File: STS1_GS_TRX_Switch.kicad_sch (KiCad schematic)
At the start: 60 parts, among them J1 SDR, J10 PA_Switch, J11 LNA_Switch, J2 From_LNA, J3 To_PA, J4 To_LNA, J5 From_PA, J6 Antenna, J7 RX_LED, J8 TX_LED, J9 5V_Supply, K1 HF3-53, K2 HF3-53, K3 HF3-53, K4 IM07, K5 IM07, Q1 BC847, Q2 BC847, Q3 BC847, Q4 BC847, Q5 BC847, U1 PC817, U2 PC817

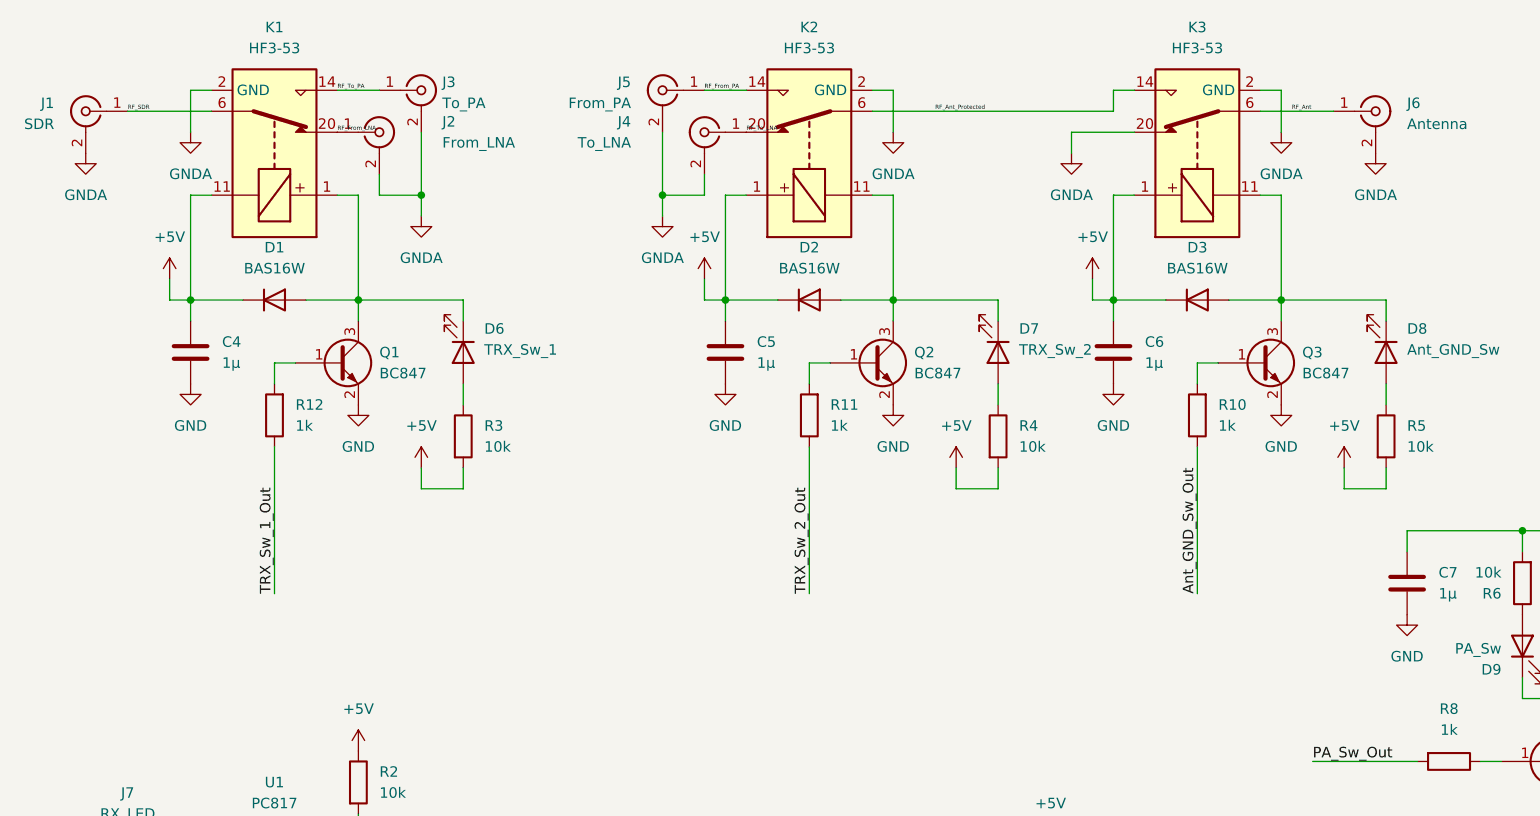
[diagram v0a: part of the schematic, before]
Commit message: fix: wrong polarity of one of the RF relays
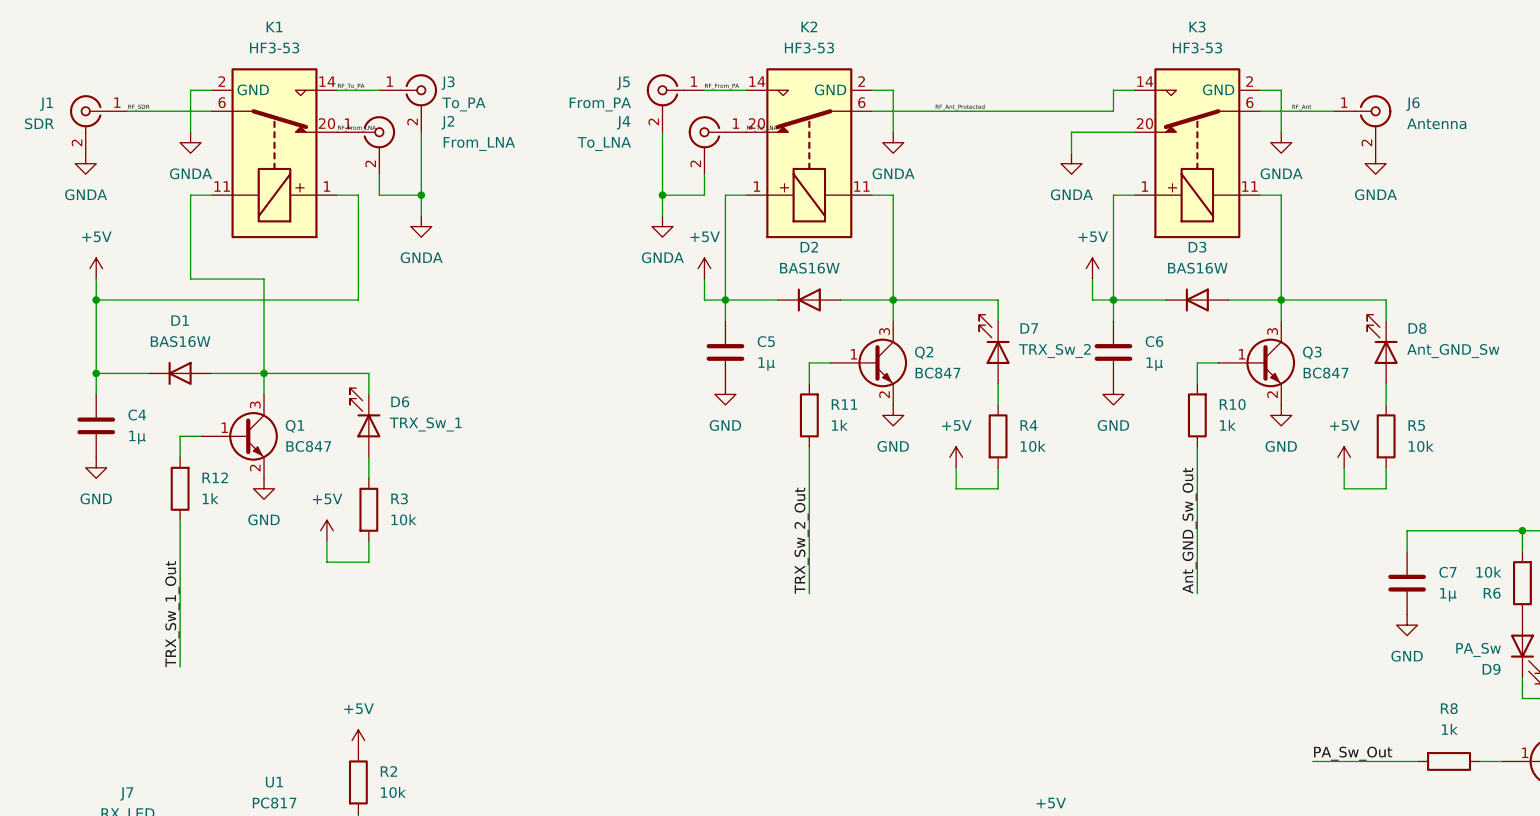
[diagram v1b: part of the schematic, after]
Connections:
- net +5V: now also K1.1; no longer K1.11
- net at D1.1 (A), D6.1 (K), Q1.3 (C): now also K1.11; no longer K1.1
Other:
- moved on the sheet: C4, D1, D6, Q1, R12, R3

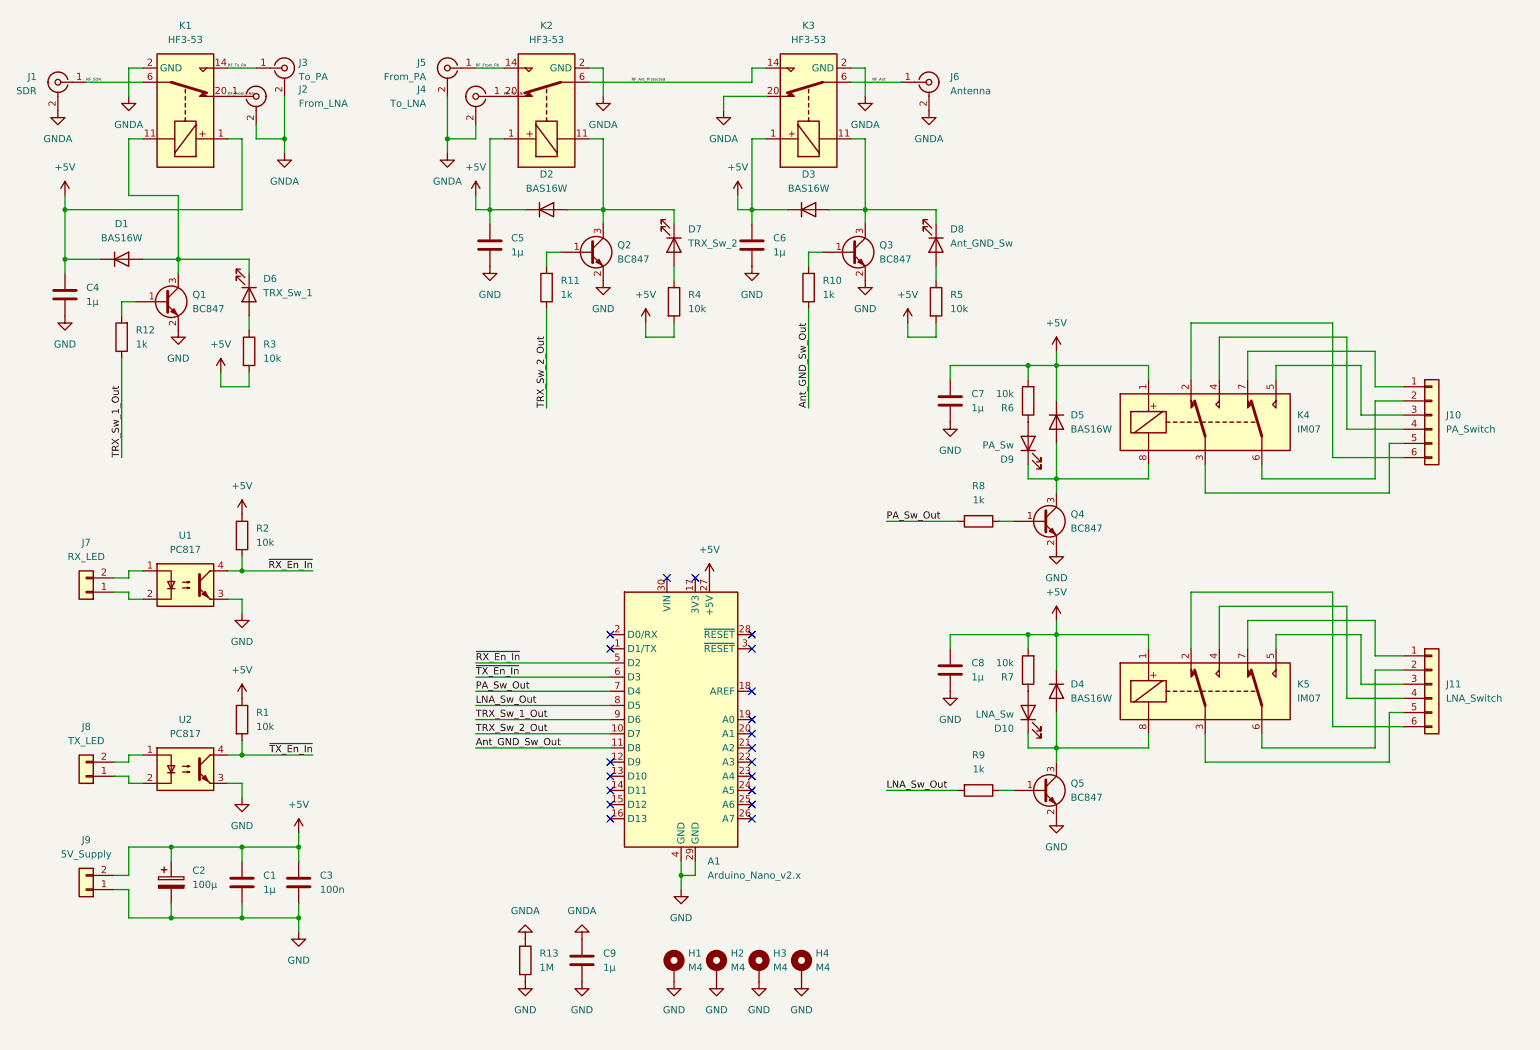
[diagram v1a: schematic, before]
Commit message: feat: v2.0 with built-in LNA, PA-pre-filter and PA output filter
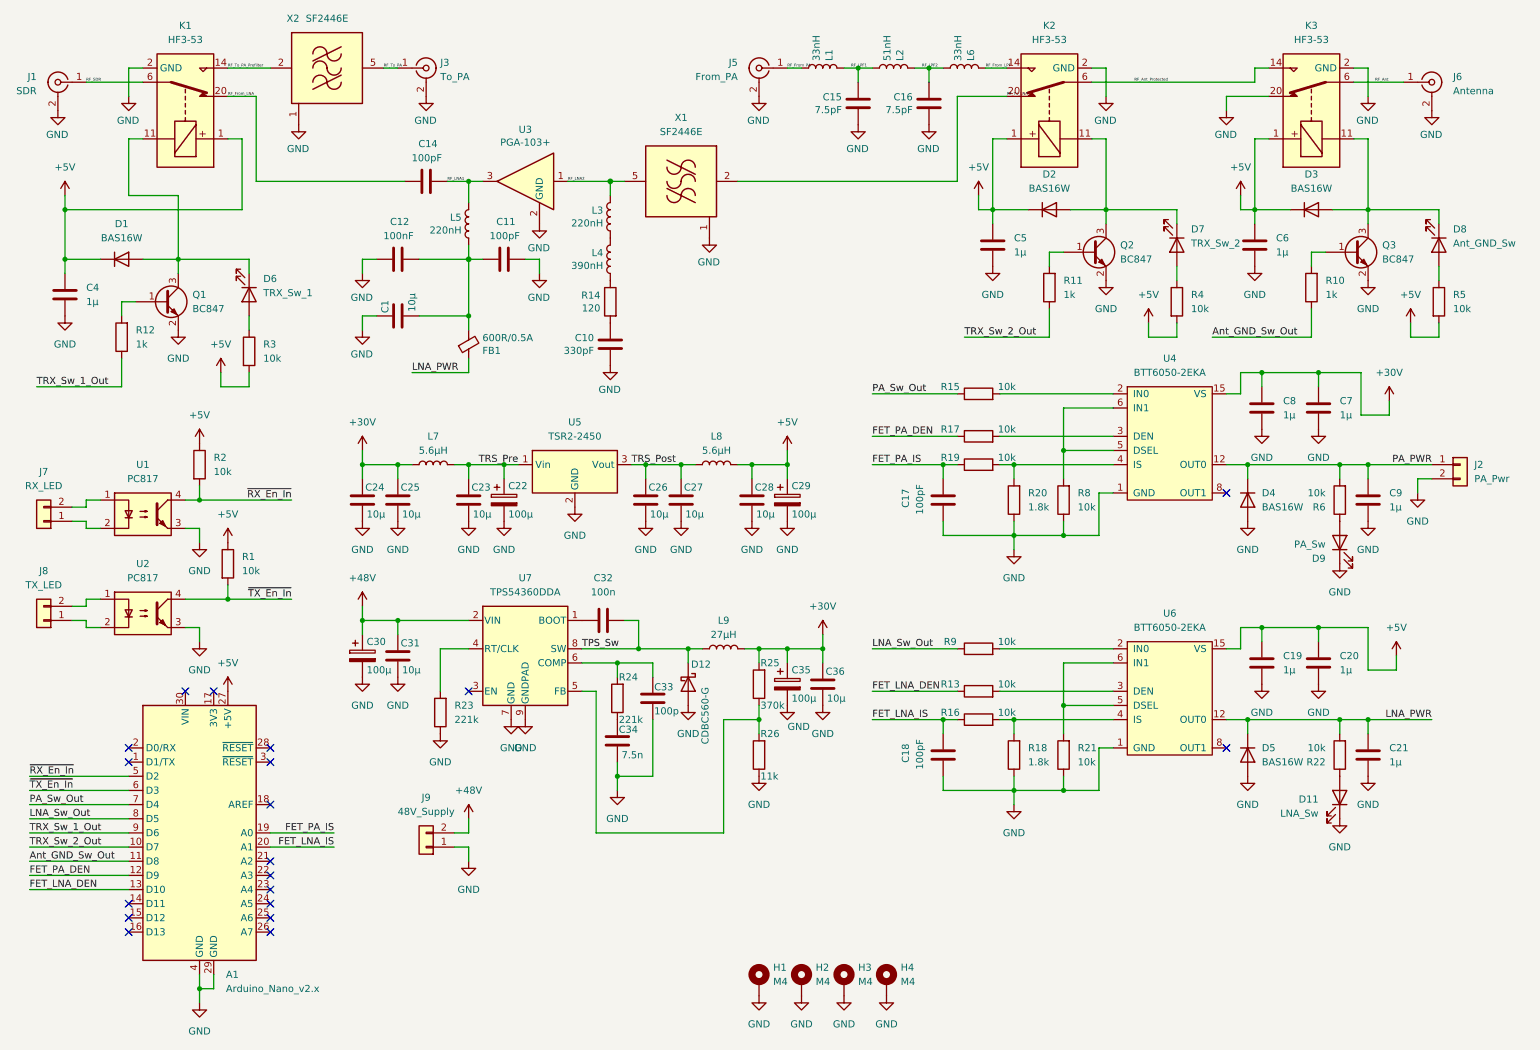
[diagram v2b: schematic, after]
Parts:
- removed C2: 100µ, Capacitor_SMD:CP_Elec_10x10, symbol Device:C_Polarized
- removed C3: 100n, Capacitor_SMD:C_0603_1608Metric_Pad1.08x0.95mm_HandSolder, symbol Device:C
- removed D10: LNA_Sw, LED_SMD:LED_1206_3216Metric_Pad1.42x1.75mm_HandSolder, symbol Device:LED
- removed J10: PA_Switch, Connector_JST:JST_XH_B6B-XH-A_1x06_P2.50mm_Vertical, symbol Connector_Generic:Conn_01x06
- removed J11: LNA_Switch, Connector_JST:JST_XH_B6B-XH-A_1x06_P2.50mm_Vertical, symbol Connector_Generic:Conn_01x06
- removed J2: From_LNA, Connector_Coaxial:SMA_Molex_73251-2120_EdgeMount_Horizontal, symbol Connector:Conn_Coaxial
- removed J4: To_LNA, Connector_Coaxial:SMA_Molex_73251-2120_EdgeMount_Horizontal, symbol Connector:Conn_Coaxial
- removed K4, K5: IM07, Relay_SMD:Relay_DPDT_AXICOM_IMSeries_JLeg, symbol Relay:IM07
- removed Q4, Q5: BC847, Package_TO_SOT_SMD:SOT-23, symbol Transistor_BJT:BC847
- removed R7: 10k, Resistor_SMD:R_0603_1608Metric_Pad0.98x0.95mm_HandSolder, symbol Device:R
- added C10: 330pF, Capacitor_SMD:C_0603_1608Metric, symbol Device:C
- added C11, C14, C17, C18: 100pF, Capacitor_SMD:C_0603_1608Metric, symbol Device:C
- added C12: 100nF, Capacitor_SMD:C_0603_1608Metric, symbol Device:C
- added C15, C16: 7.5pF, Capacitor_SMD:C_0603_1608Metric, symbol Device:C
- added C19, C20, C21: 1µ, Capacitor_SMD:C_0603_1608Metric_Pad1.08x0.95mm_HandSolder, symbol Device:C
- added C22, C29, C30, C35: 100µ, Capacitor_SMD:CP_Elec_10x10, symbol Device:C_Polarized
- added C23, C26, C27, C28, C31: 10µ, Capacitor_SMD:C_0805_2012Metric_Pad1.18x1.45mm_HandSolder, symbol Device:C
- added C24, C25, C36: 10µ, Capacitor_SMD:C_1210_3225Metric_Pad1.33x2.70mm_HandSolder, symbol Device:C
- added C32: 100n, Capacitor_SMD:C_0805_2012Metric_Pad1.18x1.45mm_HandSolder, symbol Device:C
- added C33: 100p, Capacitor_SMD:C_0603_1608Metric_Pad1.08x0.95mm_HandSolder, symbol Device:C
- added C34: 7.5n, Capacitor_SMD:C_1206_3216Metric_Pad1.33x1.80mm_HandSolder, symbol Device:C
- added D11: LNA_Sw, LED_SMD:LED_1206_3216Metric_Pad1.42x1.75mm_HandSolder, symbol Device:LED
- added D12: CDBC560-G, Diode_SMD:D_SMC_Handsoldering, symbol Device:D_Schottky
- added FB1: 600R/0.5A, fbead:Murata-BLM18-0.15-t0.8-0-0-IPC_A, symbol Device:Ferrite_Bead_Small
- added J2: PA_Pwr, Connector_JST:JST_XH_B2B-XH-A_1x02_P2.50mm_Vertical, symbol Connector_Generic:Conn_01x02
- added L1, L6: 33nH, Inductor_SMD:L_0603_1608Metric_Pad1.05x0.95mm_HandSolder, symbol Device:L
- added L2: 51nH, Inductor_SMD:L_0603_1608Metric_Pad1.05x0.95mm_HandSolder, symbol Device:L
- added L3, L5: 220nH, Inductor_SMD:L_0805_2012Metric, symbol Device:L
- added L4: 390nH, Inductor_SMD:L_0805_2012Metric, symbol Device:L
- added L7, L8: 5.6µH, Inductor_SMD:L_Abracon_ASPI-4030S, symbol Device:L
- added L9: 27µH, Inductor_SMD:L_Bourns_SRR1210A, symbol Device:L
- added R14: 120, Resistor_SMD:R_0603_1608Metric, symbol Device:R
- added R15, R16, R17, R19, R21, R22: 10k, Resistor_SMD:R_0603_1608Metric_Pad0.98x0.95mm_HandSolder, symbol Device:R
- added R18, R20: 1.8k, Resistor_SMD:R_0603_1608Metric_Pad0.98x0.95mm_HandSolder, symbol Device:R
- added R23, R24: 221k, Resistor_SMD:R_0603_1608Metric_Pad0.98x0.95mm_HandSolder, symbol Device:R
- added R25: 370k, Resistor_SMD:R_0603_1608Metric_Pad0.98x0.95mm_HandSolder, symbol Device:R
- added R26: 11k, Resistor_SMD:R_0603_1608Metric_Pad0.98x0.95mm_HandSolder, symbol Device:R
- added U3: PGA-103+, Package_TO_SOT_SMD:SOT-89-3, symbol lna_library:PGA-103+
- added U4, U6: BTT6050-2EKA, btt6050-2eka:Infineon_PG-DSO-14-40-EP_3.9x8.65mm_P1.27mm, symbol btt6050-2eka:BTT6050-2EKA
- added U5: TSR2-2450, Converter_DCDC:Converter_DCDC_TRACO_TSR2-xxxx_THT, symbol Regulator_Switching:TSR2-2450
- added U7: TPS54360DDA, Package_SO:TI_SO-PowerPAD-8_ThermalVias, symbol Regulator_Switching:TPS54360DDA
- added X1, X2: SF2446E, saw:Filter_SAW-6_3.0x3.0mm, symbol RF_Filter:STA1090EC
- C1: value 1µ -> 10µ; footprint Capacitor_SMD:C_0603_1608Metric_Pad1.08x0.95mm_HandSolder -> Capacitor_SMD:C_1210_3225Metric_Pad1.33x2.70mm_HandSolder
- J1, J3, J5, J6: footprint Connector_Coaxial:SMA_Molex_73251-2120_EdgeMount_Horizontal -> SMA:SMA_Molex_73251-2120_EdgeMount_Horizontal
- J9: value 5V_Supply -> 48V_Supply
- R13: value 1M -> 10k
- R8, R9: value 1k -> 10k
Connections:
- net +5V: now also C19.1, C20.1, C28.1, C29.1, L8.2, U6.15 (VS); no longer C1.1, C7.1, C8.1, D4.3 (K), D5.3 (K), J9.2 (Pin_2), R6.2
- net GND: now also C1.1, D4.1 (A), D5.1 (A), D9.1 (K), J1.2 (Ext), J3.2 (Ext), J5.2 (Ext), J6.2 (Ext), K1.10 (GND), K1.12 (GND), K1.13 (GND), K1.15 (GND), K1.17 (GND), K1.19 (GND), K1.2 (GND), K1.21 (GND), K1.22 (GND), K1.5 (GND), K1.7 (GND), K2.10 (GND), K2.12 (GND), K2.13 (GND), K2.15 (GND), K2.17 (GND), K2.19 (GND), K2.2 (GND), K2.21 (GND), K2.22 (GND), K2.5 (GND), K2.7 (GND), K3.10 (GND), K3.12 (GND), K3.13 (GND), K3.15 (GND), K3.17 (GND), K3.19 (GND), K3.2 (GND), K3.20, K3.21 (GND), K3.22 (GND), K3.5 (GND), K3.7 (GND), R8.1, C10.2, C11.1, C12.2, C15.2, C16.2, C17.2, C18.2, C19.2, C20.2, C21.2, C22.2, C23.2, C24.2, C25.2, C26.2, C27.2, C28.2, C29.2, C30.2, C31.2, C33.2, C34.2, C35.2, C36.2, D11.1 (K), D12.2 (A), J2.2 (Pin_2), R18.1, R20.1, R21.1, R23.1, R26.1, U3.2 (GND), U4.1 (GND), U5.2 (GND), U6.1 (GND), U7.7 (GND), U7.9 (GNDPAD), X1.1 (GND), X1.3 (GND), X1.4 (GND), X1.6 (GND), X2.1 (GND), X2.3 (GND), X2.4 (GND), X2.6 (GND); no longer C1.2, R13.2
- net LNA_Sw_Out: now also R9.1; no longer R9.2
- net PA_Sw_Out: now also R15.1; no longer R8.2
- net RF_From_LNA: now also C14.2
- net RF_From_PA: now also L1.2; no longer K2.14
- net RF_To_LNA: now also X1.2 (IN)
- net RF_To_PA: now also X2.5 (OUT); no longer K1.14
- net FET_PA_DEN: now reaches A1.12 (D9)
- net FET_PA_DEN: now also R17.1
- net FET_LNA_DEN: now reaches A1.13 (D10)
- net FET_LNA_DEN: now also R13.1
- net FET_PA_IS: now reaches A1.19 (A0)
- net FET_PA_IS: now also C17.1, R19.1
- net FET_LNA_IS: now reaches A1.20 (A1)
- net FET_LNA_IS: now also C18.1, R16.1
- removed net GNDA: C9.1, J1.2 (Ext), J3.2 (Ext), J5.2 (Ext), J6.2 (Ext), K1.10 (GND), K1.12 (GND), K1.13 (GND), K1.15 (GND), K1.17 (GND), K1.19 (GND), K1.2 (GND), K1.21 (GND), K1.22 (GND), K1.5 (GND), K1.7 (GND), K2.10 (GND), K2.12 (GND), K2.13 (GND), K2.15 (GND), K2.17 (GND), K2.19 (GND), K2.2 (GND), K2.21 (GND), K2.22 (GND), K2.5 (GND), K2.7 (GND), K3.10 (GND), K3.12 (GND), K3.13 (GND), K3.15 (GND), K3.17 (GND), K3.19 (GND), K3.2 (GND), K3.20, K3.21 (GND), K3.22 (GND), K3.5 (GND), K3.7 (GND), R13.1
- new net: C1.2, C11.2, C12.1, FB1.2, L5.2
- new net: R16.2, R18.2, U6.4 (IS)
- new net: R8.2, U4.5 (DSEL), U4.6 (IN1)
- new net: R19.2, R20.2, U4.4 (IS)
- new net: D11.2 (A), R22.1
- new net: R13.2, U6.3 (DEN)
- new net: C34.1, R24.1
- new net: C33.1, R24.2, U7.6 (COMP)
- new net: R21.2, U6.5 (DSEL), U6.6 (IN1)
- new net: R17.2, U4.3 (DEN)
- new net: L4.2, R14.1
- new net: C10.1, R14.2
- new net: R9.2, U6.2 (IN0)
- new net: C32.1, U7.1 (BOOT)
- new net: R23.2, U7.4 (RT/CLK)
- new net: R25.1, R26.2, U7.5 (FB)
- new net: U4.10 (OUT1), U4.8 (OUT1), U4.9 (OUT1)
- new net: R15.2, U4.2 (IN0)
- new net: U6.10 (OUT1), U6.8 (OUT1), U6.9 (OUT1)
- new net: L3.2, L4.1
- new net +30V: C24.1, C25.1, C35.1, C36.1, C7.1, C8.1, L7.1, L9.2, R25.2, U4.15 (VS)
- new net +48V: C30.1, C31.1, J9.2 (Pin_2), U7.2 (VIN)
- new net LNA_PWR: C21.1, D5.3 (K), FB1.1, R22.2, U6.12 (OUT0), U6.13 (OUT0), U6.14 (OUT0)
- new net PA_PWR: C9.1, D4.3 (K), J2.1 (Pin_1), R6.2, U4.12 (OUT0), U4.13 (OUT0), U4.14 (OUT0)
- new net RF_From_LPF: K2.14, L6.1
- new net RF_LNA1: C14.1, L5.1, U3.3
- new net RF_LNA2: L3.1, U3.1, X1.5 (OUT)
- new net RF_LPF1: C15.1, L1.1, L2.2
- new net RF_LPF2: C16.1, L2.1, L6.2
- new net RF_To_PA_Prefilter: K1.14, X2.2 (IN)
- new net TPS_Sw: C32.2, D12.1 (K), L9.1, U7.8 (SW)
- new net TRS_Post: C26.1, C27.1, L8.1, U5.3 (Vout)
- new net TRS_Pre: C22.1, C23.1, L7.2, U5.1 (Vin)
- no-connect marks 20 -> 19
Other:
- moved on the sheet: A1, C5, C6, C7, C8, D2, D3, D4, D7, D8, D9, H1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
